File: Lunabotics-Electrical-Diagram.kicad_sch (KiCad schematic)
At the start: 3 parts, among them J1 PDB_Mains, J2 PDB_CAN, J3 Talon

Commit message: Finsihed V1
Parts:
- removed J1: PDB_Mains, symbol Connector_Generic:Conn_02x16_Counter_Clockwise
- removed J2: PDB_CAN, symbol Connector_Generic:Conn_01x04
- removed J3: Talon, symbol Connector_Generic:Conn_02x04_Counter_Clockwise
- added J1: 8_40A_Channels, symbol Connector_Generic:Conn_02x08_Counter_Clockwise
- added J10, J13, J17, J21: MC_CAN_I, symbol Connector_Generic:Conn_01x02
- added J11, J15, J19, J23: MC_CAN_O, symbol Connector_Generic:Conn_01x02
- added J12, J16, J20, J8: MC_In, symbol Connector_Generic:Conn_01x02
- added J14, J18, J22, J9: MC_Out, symbol Connector_Generic:Conn_01x02
- added J2: 8_30A/20A_Channels, symbol Connector_Generic:Conn_02x08_Counter_Clockwise
- added J24: THD-20-R, Connector_PinHeader_2.54mm:PinHeader_2x20_P2.54mm_Vertical, symbol Connector_Generic:Conn_02x20_Odd_Even
- added J25: RPI_USBC, symbol Connector_Generic:Conn_01x01
- added J26: CAN Hat Channel 1, symbol Connector_Generic:Conn_01x03
- added J27: CAN Hat Channel 2, symbol Connector_Generic:Conn_01x03
- added J28: 5V/2A, symbol Connector_Generic:Conn_01x04
- added J29: 12V/500mA, symbol Connector_Generic:Conn_01x04
- added J3: Main_Power, symbol Connector_Generic:Conn_01x02
- added J30: 5V/500mA, symbol Connector_Generic:Conn_01x04
- added J31: VRM_In, symbol Connector_Generic:Conn_01x02
- added J32: Conn_01x06, symbol Connector_Generic:Conn_01x06
- added J4: CAN_Bus, symbol Connector_Generic:Conn_01x04
- added J5: Buck_In, symbol Connector_Generic:Conn_01x02
- added J6: 12V/2A, symbol Connector_Generic:Conn_01x04
- added J7: 5V_Buck_USBC, symbol Connector_Generic:Conn_01x01
- added M1, M5, M6, M7, M8, M9: D_CIM_2, symbol Motor:Motor_DC
- added M2: D_CIM_4, symbol Motor:Motor_DC
- added M3: D_CIM_1, symbol Motor:Motor_DC
- added M4: D_CIM_3, symbol Motor:Motor_DC
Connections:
- new net: J22.2 (Pin_2), M4.1 (+)
- new net: J22.1 (Pin_1), M4.2 (-)
- new net: J9.2 (Pin_2), M1.1 (+)
- new net: J9.1 (Pin_1), M1.2 (-)
- new net: J31.2 (Pin_2), J32.1 (Pin_1)
- new net: J31.1 (Pin_1), J32.2 (Pin_2)
- new net: J14.1 (Pin_1), M2.2 (-)
- new net: J14.2 (Pin_2), M2.1 (+)
- new net: J18.1 (Pin_1), M3.2 (-)
- new net: J18.2 (Pin_2), M3.1 (+)
- new net +3.3v: J24.1 (Pin_1), J24.17 (Pin_17)
- new net +5v: J24.2 (Pin_2), J24.4 (Pin_4)
- new net 5V_Buck: J25.1 (Pin_1), J7.1 (Pin_1)
- new net CAN_G_1: J26.1 (Pin_1)
- new net CAN_G_2: J27.1 (Pin_1)
- new net CAN_H: J11.2 (Pin_2), J13.1 (Pin_1), J15.2 (Pin_2), J17.1 (Pin_1), J19.2 (Pin_2), J21.1 (Pin_1)
- new net CAN_H_1: J26.3 (Pin_3)
- new net CAN_H_2: J23.2 (Pin_2), J27.3 (Pin_3)
- new net CAN_L: J11.1 (Pin_1), J13.2 (Pin_2), J15.1 (Pin_1), J17.2 (Pin_2), J19.1 (Pin_1), J21.2 (Pin_2)
- new net CAN_L_1: J26.2 (Pin_2)
- new net CAN_L_2: J23.1 (Pin_1), J27.2 (Pin_2)
- new net GND: J24.14 (Pin_14), J24.20 (Pin_20), J24.25 (Pin_25), J24.30 (Pin_30), J24.34 (Pin_34), J24.39 (Pin_39), J24.6 (Pin_6), J24.9 (Pin_9)
- new net GPIO10: J24.19 (Pin_19)
- new net GPIO11: J24.23 (Pin_23)
- new net GPIO12: J24.32 (Pin_32)
- new net GPIO13: J24.33 (Pin_33)
- new net GPIO14: J24.8 (Pin_8)
- new net GPIO15: J24.10 (Pin_10)
- new net GPIO16: J24.36 (Pin_36)
- new net GPIO17: J24.11 (Pin_11)
- new net GPIO18: J24.12 (Pin_12)
- new net GPIO19: J24.35 (Pin_35)
- new net GPIO2: J24.3 (Pin_3)
- new net GPIO20: J24.38 (Pin_38)
- new net GPIO21: J24.40 (Pin_40)
- new net GPIO22: J24.15 (Pin_15)
- new net GPIO23: J24.16 (Pin_16)
- new net GPIO24: J24.18 (Pin_18)
- new net GPIO25: J24.22 (Pin_22)
- new net GPIO26: J24.37 (Pin_37)
- new net GPIO27: J24.13 (Pin_13)
- new net GPIO3: J24.5 (Pin_5)
- new net GPIO4: J24.7 (Pin_7)
- new net GPIO5: J24.29 (Pin_29)
- new net GPIO6: J24.31 (Pin_31)
- new net GPIO7: J24.26 (Pin_26)
- new net GPIO8: J24.24 (Pin_24)
- new net GPIO9: J24.21 (Pin_21)
- new net ID_SC: J24.28 (Pin_28)
- new net ID_SD: J24.27 (Pin_27)
- new net PD_CAN_H: J10.1 (Pin_1), J4.2 (Pin_2), J4.4 (Pin_4)
- new net PD_CAN_L: J10.2 (Pin_2), J4.1 (Pin_1), J4.3 (Pin_3)
- new net VBAT+: J1.10 (Pin_10), J1.12 (Pin_12), J1.14 (Pin_14), J1.16 (Pin_16), J1.2 (Pin_2), J1.4 (Pin_4), J1.6 (Pin_6), J1.8 (Pin_8), J12.1 (Pin_1), J16.1 (Pin_1), J2.10 (Pin_10), J2.12 (Pin_12), J2.14 (Pin_14), J2.16 (Pin_16), J2.2 (Pin_2), J2.4 (Pin_4), J2.6 (Pin_6), J2.8 (Pin_8), J20.1 (Pin_1), J3.1 (Pin_1), J5.1 (Pin_1), J8.1 (Pin_1)
- new net VBAT-: J1.1 (Pin_1), J1.11 (Pin_11), J1.13 (Pin_13), J1.15 (Pin_15), J1.3 (Pin_3), J1.5 (Pin_5), J1.7 (Pin_7), J1.9 (Pin_9), J12.2 (Pin_2), J16.2 (Pin_2), J2.1 (Pin_1), J2.11 (Pin_11), J2.13 (Pin_13), J2.15 (Pin_15), J2.3 (Pin_3), J2.5 (Pin_5), J2.7 (Pin_7), J2.9 (Pin_9), J20.2 (Pin_2), J3.2 (Pin_2), J5.2 (Pin_2), J8.2 (Pin_2)
- new net VBAT_CONT+: J32.5 (Pin_5)
- new net VBAT_CONT-: J32.6 (Pin_6)
- new net VBAT_PCM+: J32.3 (Pin_3)
- new net VBAT_PCM-: J32.4 (Pin_4)
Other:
- note added: "40Way GPIO Header"
- note added: "5V/5A Buck Converter (USB-C Out)"
- note added: "Bucket Motor"
- note added: "Bucket System Linear Actuators"
- note added: "CTRE VRM"
- note added: "Conveyor Belt"
- note added: "Drive Train Motors"
- note added: "Generic Motor Controller"
- note added: "Hatch"
- note added: "Power Distribution Panel"
- note added: "RPI5 and Waveshare CAN Hat"
- note added: "The remaining motors in this section would likewise interface with their respective motor controllers. They're omitted here to preserve clarity and avoid clutter in the schematic."

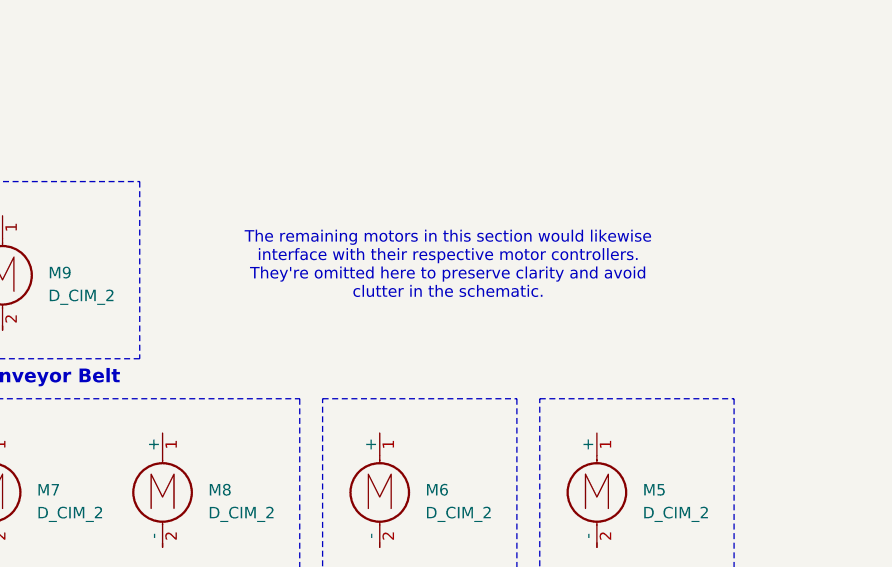
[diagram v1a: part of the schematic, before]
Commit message: Update page settings
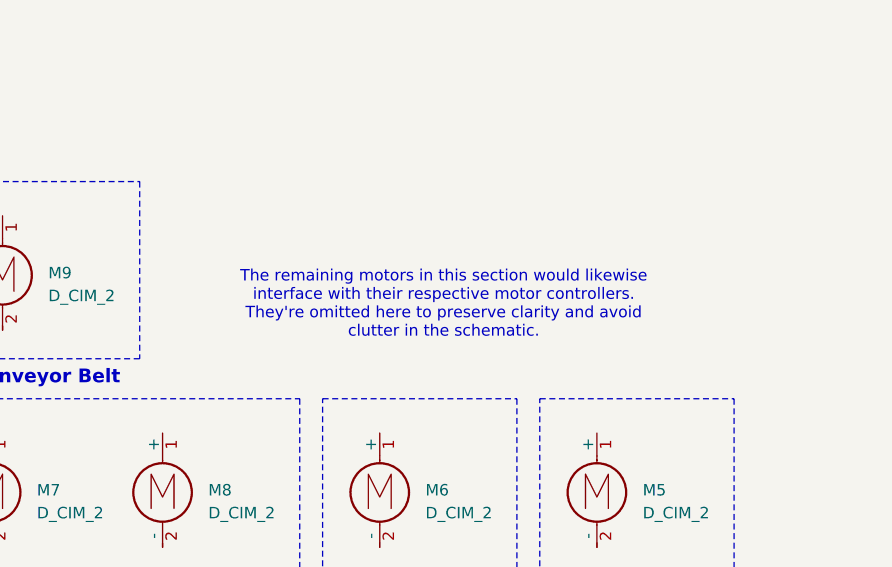
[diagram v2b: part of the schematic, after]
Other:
- company: (none) -> Rutgers STAR
- title: (none) -> Lunabotics Rover 2 Electrical Diagram
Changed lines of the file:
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@@
 	(generator_version "9.0")
 	(paper "A4")
+	(title_block
+		(title "Lunabotics Rover 2 Electrical Diagram")
+		(date "2025-12-03")
+		(rev "1")
+		(company "Rutgers STAR")
+	)
 	(rectangle
 		(start 96.52 82.296)
@@
 	(text "The remaining motors in this section would likewise \ninterface with their respective motor controllers.\nThey're omitted here to preserve clarity and avoid \nclutter in the schematic."
 		(exclude_from_sim no)
-		(at 143.51 159.258 0)
-		(effects
-			(font
+		(at 143.002 163.576 0)
+		(effects
+			(font
